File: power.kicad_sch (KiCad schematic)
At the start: 30 parts, among them J1 USB_C Connector, J3 START_MODULE, J6 BATT_IN, Q1 Si2371EDS, U1 LMR33630ADDAR, U2 USBLC6-2P6, U4 TLV75733PDBVR

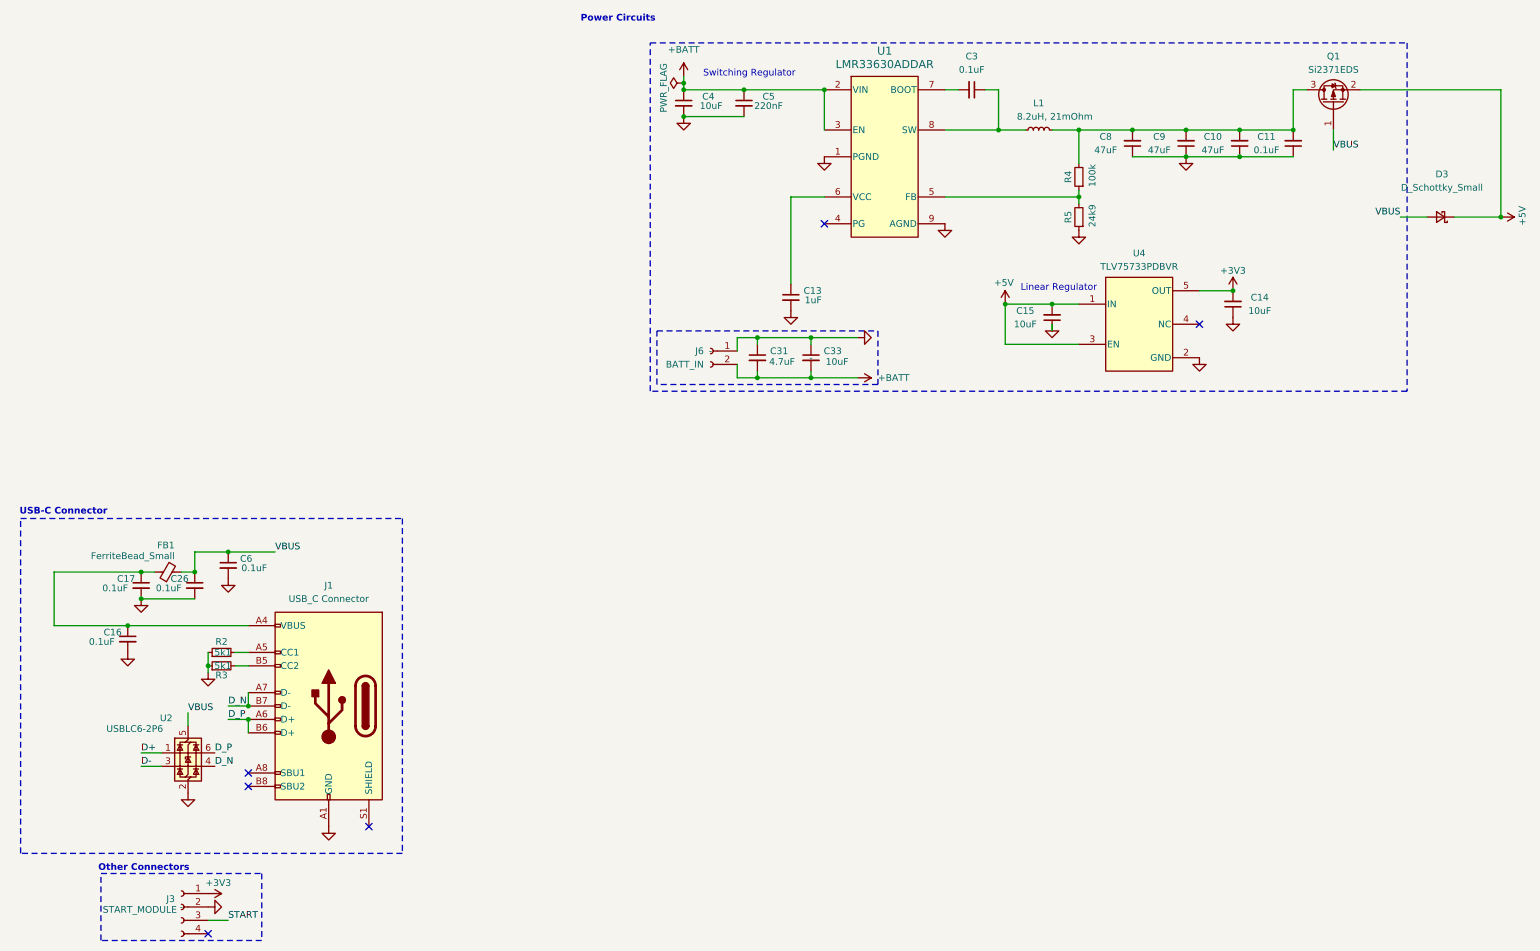
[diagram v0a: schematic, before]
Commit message: added global labels
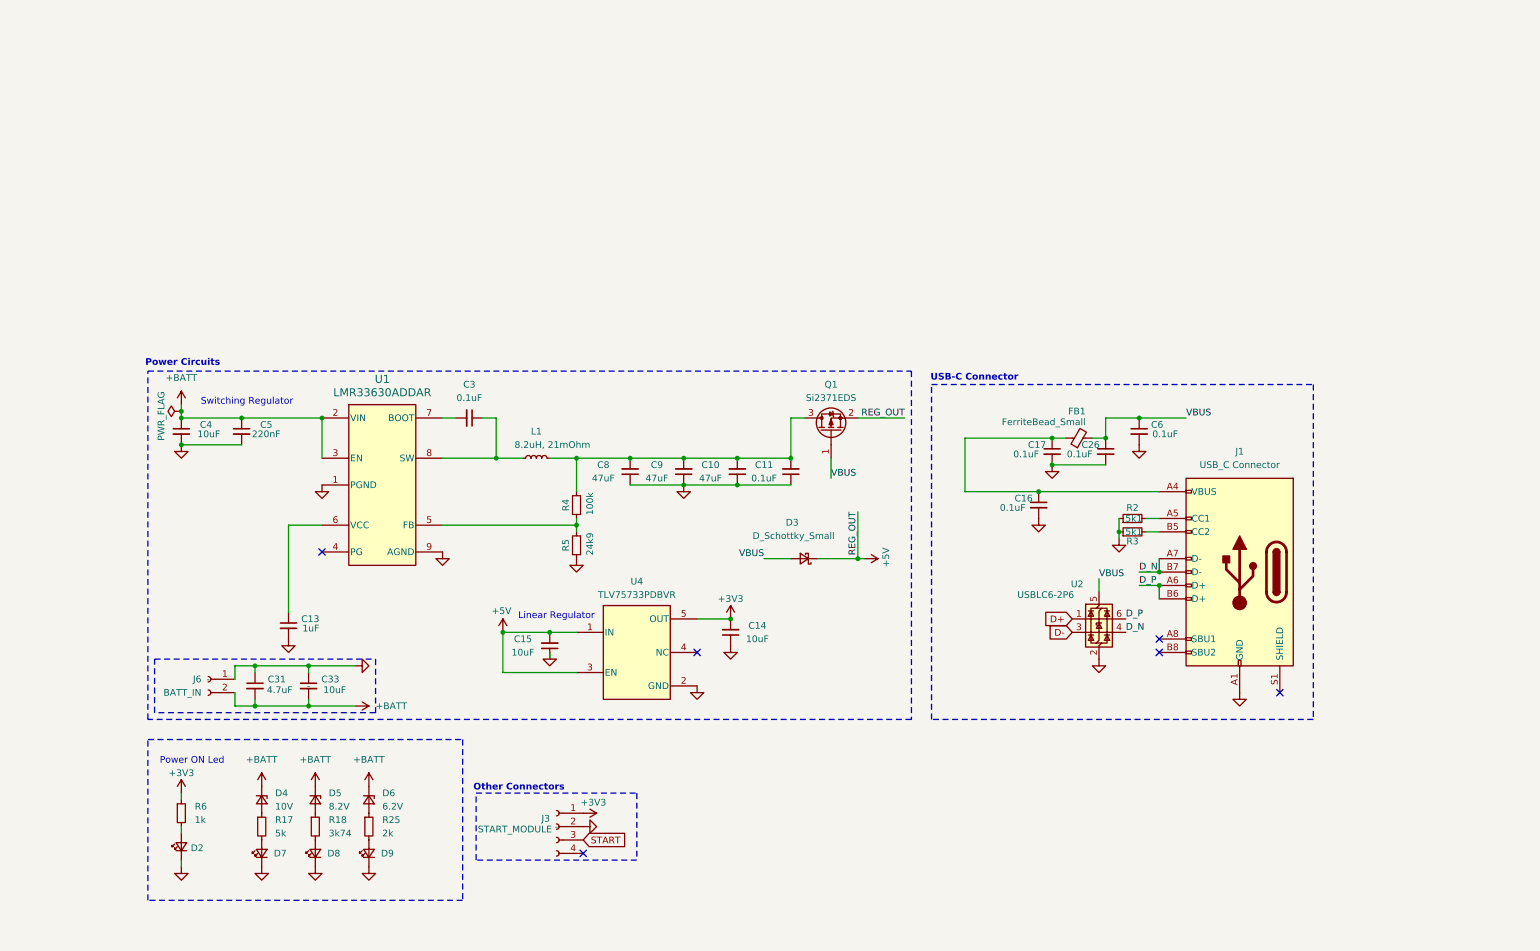
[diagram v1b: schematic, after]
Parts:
- added D2, D7, D8, D9: 1.95Vf, 20mA, RED, LED_SMD:LED_0603_1608Metric, symbol Device:LED_Small
- added D4: 10V, Diode_SMD:D_SOD-123F, symbol Device:D_Zener_Small
- added D5: 8.2V, Diode_SMD:D_SOD-123F, symbol Device:D_Zener_Small
- added D6: 6.2V, Diode_SMD:D_SOD-123F, symbol Device:D_Zener_Small
- added R17: 5k, Resistor_SMD:R_0603_1608Metric, symbol Device:R_Small
- added R18: 3k74, Resistor_SMD:R_0603_1608Metric, symbol Device:R_Small
- added R25: 2k, Resistor_SMD:R_0603_1608Metric, symbol Device:R_Small
- added R6: 1k, Resistor_SMD:R_0603_1608Metric, symbol Device:R_Small
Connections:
- net +3V3: now also R6.1
- net +BATT: now also D4.1 (K), D5.1 (K), D6.1 (K)
- net GND: now also D2.1 (K), D7.1 (K), D8.1 (K), D9.1 (K)
- new net: D5.2 (A), R18.1
- new net: D8.2 (A), R18.2
- new net: D6.2 (A), R25.1
- new net: D4.2 (A), R17.1
- new net: D7.2 (A), R17.2
- new net: D9.2 (A), R25.2
- new net: D2.2 (A), R6.2
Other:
- note added: "Power ON Led"
- moved on the sheet: C10, C11, C13, C14, C15, C16, C17, C26, C3, C31, C33, C4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

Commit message: added PDFs
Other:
- title: (none) -> Minisumo PCB
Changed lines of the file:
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@@
 	(generator_version "9.0")
 	(paper "A4")
+	(title_block
+		(title "Minisumo PCB")
+		(date "2025-04-16")
+		(rev "3.2")
+		(comment 2 "alex_ivan1304@outlook.com")
+		(comment 3 "Designed by: Ivan Alexandru Marian")
+	)
 	(rectangle
 		(start 39.37 107.95)

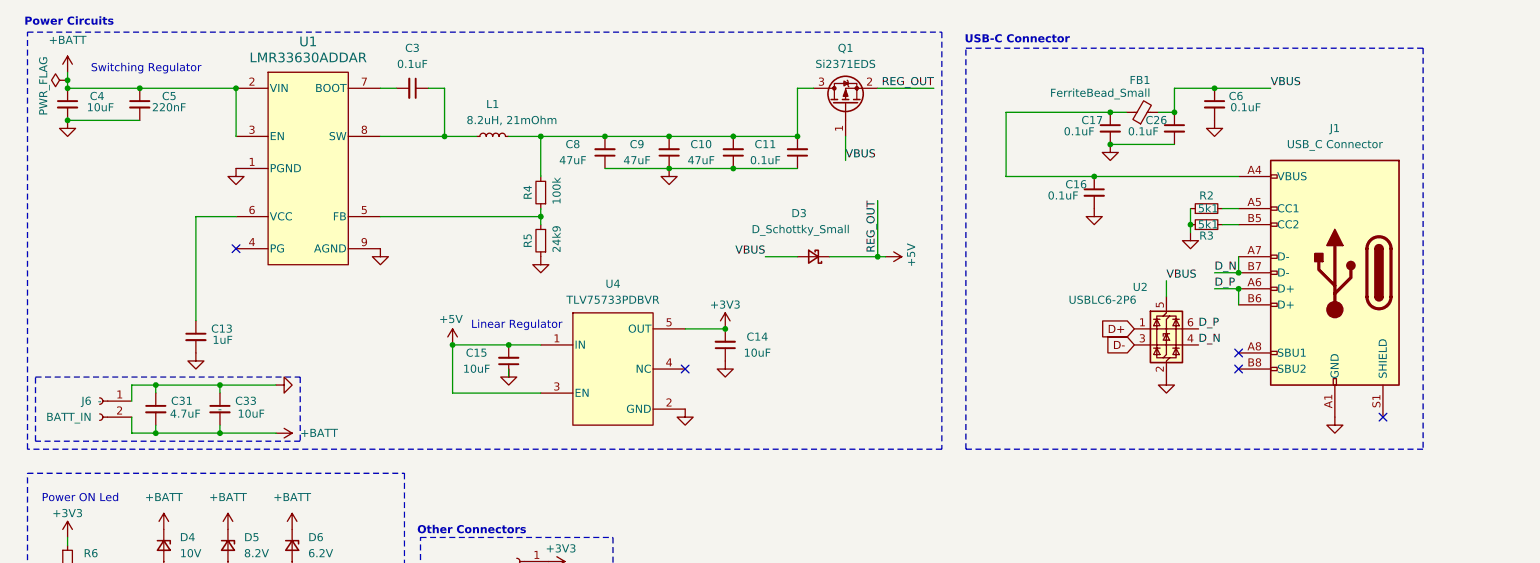
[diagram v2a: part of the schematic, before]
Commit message: added test pads and gate resistor for PMOS
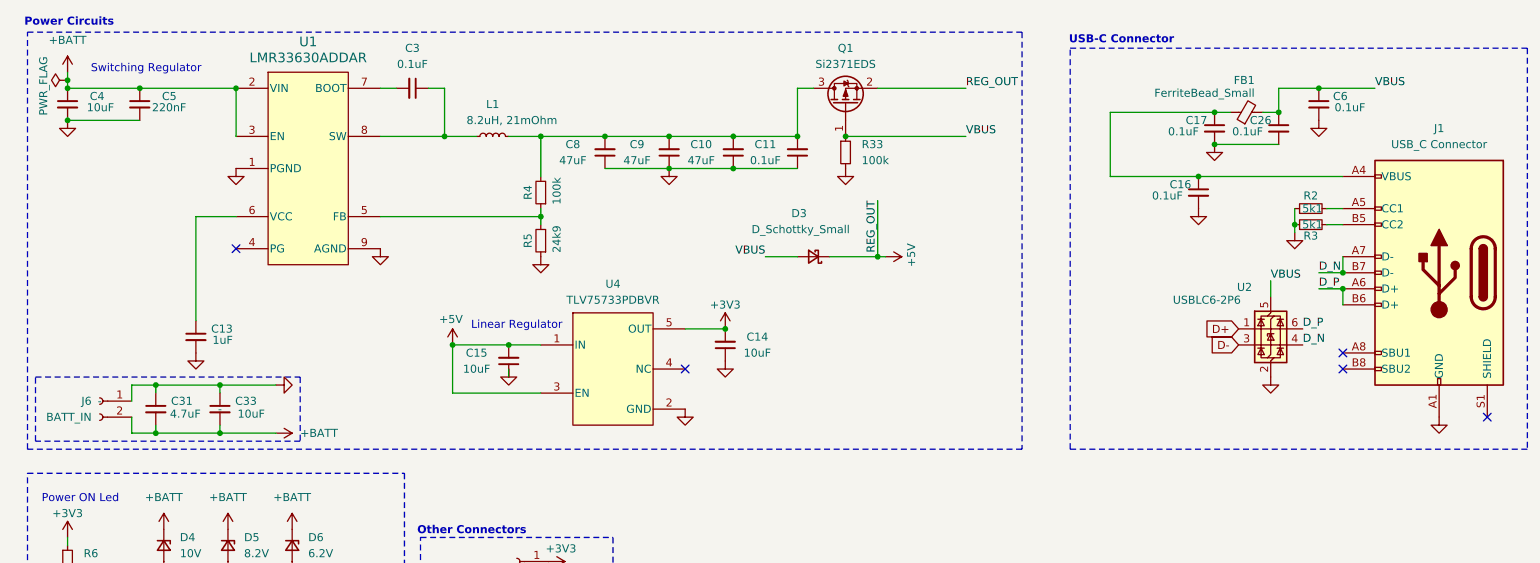
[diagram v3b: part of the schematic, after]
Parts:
- added R33: 100k, Resistor_SMD:R_0603_1608Metric, symbol Device:R_Small
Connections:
- net GND: now also R33.2
- net VBUS: now also R33.1
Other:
- moved on the sheet: C16, C17, C26, C6, FB1, J1, R2, R3, U2

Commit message: custom
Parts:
- added C35: 4.7uF, Capacitor_SMD:C_0603_1608Metric, symbol Device:C_Small
- added C36: 1uF, Capacitor_SMD:C_0603_1608Metric, symbol Device:C_Small
- C31: value 4.7uF -> 47uF; footprint Capacitor_SMD:C_0603_1608Metric -> Capacitor_SMD:C_1210_3225Metric; LCSC Part # C437568 -> C77101; M_NUMBER 81-GRM188R6YA475KE5D -> 81-GRM32ER61C476KE5L
- C33: footprint Capacitor_THT:C_Radial_D6.3mm_H11.0mm_P2.50mm -> Capacitor_SMD:C_0603_1608Metric; M_NUMBER - -> 810-CGA3EDX7T1A106M0
- L1: footprint Inductor_SMD:L_Coilcraft_XAL4040-XXX -> footprints:INDPM7166X300N; M_NUMBER 994-XAL4040-822MEC -> 652-SRP6530A-8R2M
- R17: value 5k -> 10k
- R18: value 3k74 -> 10k
- R25: value 2k -> 10k
- R6: value 1k -> 10k
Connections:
- net +BATT: now also C35.2, C36.2
- net GND: now also C35.1, C36.1
